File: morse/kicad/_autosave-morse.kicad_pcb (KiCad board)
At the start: 2 copper layers, 63.5 x 63.5 mm, 14 parts, among them J1 Conn_01x04, Q1 2N2219, Q2 2N2219

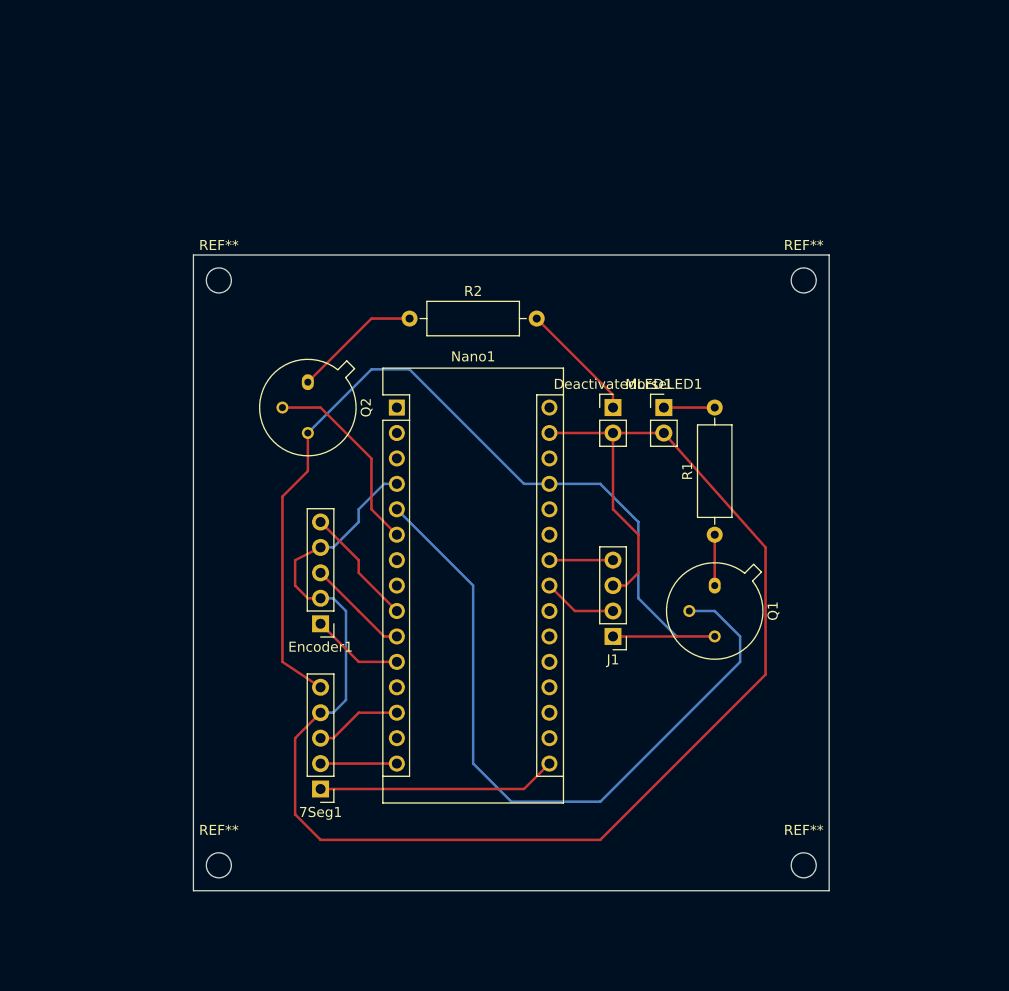
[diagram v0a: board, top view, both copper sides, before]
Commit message: updating maze symlinks and added rotary encoder to kicad
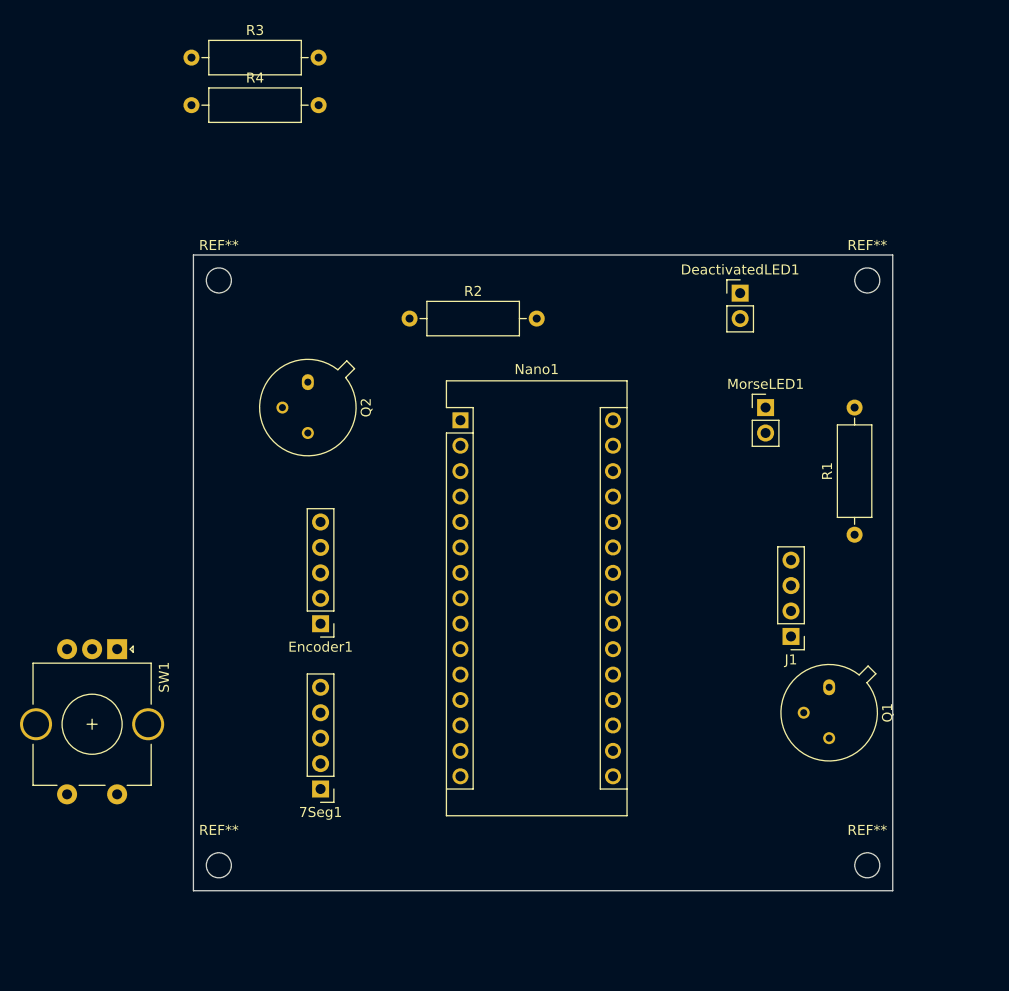
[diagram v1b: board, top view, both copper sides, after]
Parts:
- added R3: R, Resistor_THT:R_Axial_DIN0309_L9.0mm_D3.2mm_P12.70mm_Horizontal, F.Cu at (133.2, 51.4)
- added R4: R, Resistor_THT:R_Axial_DIN0309_L9.0mm_D3.2mm_P12.70mm_Horizontal, F.Cu at (133.2, 56.2)
- added SW1: Rotary_Encoder_Switch, Rotary_Encoder:RotaryEncoder_Alps_EC11E-Switch_Vertical_H20mm_CircularMountingHoles, F.Cu at (125.7, 110.5)
- moved J1 17.8 mm to (193.0, 109.2)
- moved DeactivatedLED1 17.1 mm to (188.0, 74.9)
- moved Q1 15.3 mm to (196.8, 114.3)
- moved R1 14.0 mm to (199.4, 99.1)
- moved MorseLED1 10.2 mm to (190.5, 86.4)
- moved Nano1 6.48 mm to (160.0, 87.6)
- moved REF** 6.35 mm to (200.7, 132.1)
- moved REF** 6.35 mm to (200.7, 73.7)
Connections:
- Nano1 pad 10: Net-(Encoder1-Pad3) -> Net-(Nano1-Pad10)
- Nano1 pad 11: Net-(Encoder1-Pad1) -> Net-(Nano1-Pad11)
- Nano1 pad 9: Net-(Encoder1-Pad5) -> Net-(Nano1-Pad9)
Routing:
- net GND: track 158.1 -> 0.00 mm
- net +5V: track 97.4 -> 0.00 mm
- net Net-(Nano1-Pad5): track 71.3 -> 0.00 mm
- net Net-(7Seg1-Pad1): track 23.9 -> 0.00 mm
- net Net-(Nano1-Pad6): track 19.7 -> 0.00 mm
- net Net-(Q2-Pad1): track 12.8 -> 0.00 mm
- net Net-(DeactivatedLED1-Pad1): track 12.0 -> 0.00 mm
- net Net-(Encoder1-Pad5): track 12.0 -> 0.00 mm
- net Net-(Encoder1-Pad3): track 10.3 -> 0.00 mm
- net Net-(Encoder1-Pad1): track 9.20 -> 0.00 mm
- net Net-(7Seg1-Pad3): track 8.67 -> 0.00 mm
- net Net-(7Seg1-Pad2): track 7.62 -> 0.00 mm
- net Net-(J1-Pad2): track 7.40 -> 0.00 mm
- net Net-(J1-Pad4): track 6.35 -> 0.00 mm
- net Net-(Q1-Pad1): track 5.08 -> 0.00 mm
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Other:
- board size 63.5 x 63.5 mm -> 69.8 x 63.5 mm

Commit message: started adding knob module, started adding timing into master
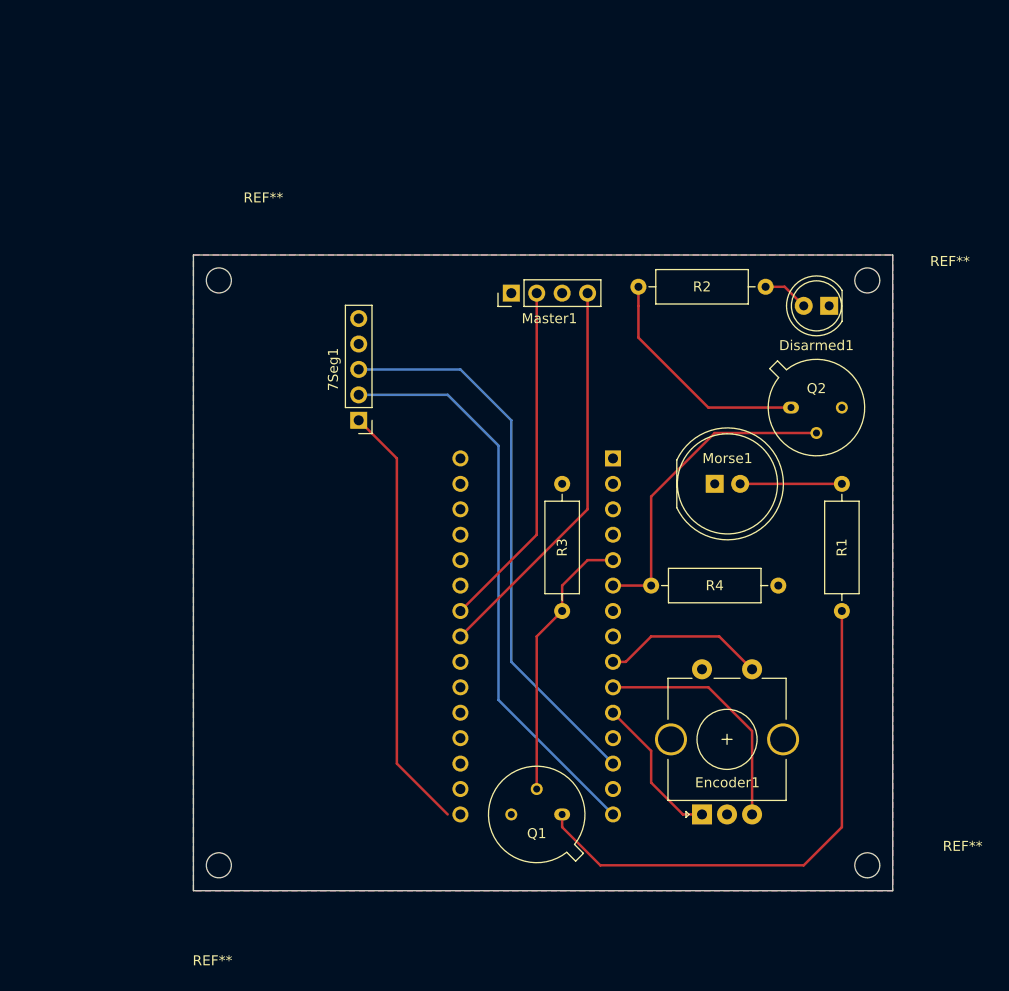
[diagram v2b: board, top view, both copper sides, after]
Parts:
- removed DeactivatedLED1, MorseLED1: Conn_01x02, Connector_PinHeader_2.54mm:PinHeader_1x02_P2.54mm_Vertical
- removed the Encoder1 at (146.1, 108.0)
- added Disarmed1: LED, LED_THT:LED_D5.0mm, F.Cu at (196.8, 76.2)
- added Morse1: LED, LED_THT:LED_D10.0mm, F.Cu at (185.4, 94.0)
- Nano1: moved to B.Cu
- moved R3 66.5 mm to (170.2, 106.7), turned to 90 degrees
- moved R4 66.4 mm to (179.1, 104.1)
- moved Encoder1 60.7 mm to (184.2, 127.0), turned to 90 degrees
- moved Q2 48.3 mm to (193.0, 86.4), turned to 0 degrees
- moved Master1 44.2 mm to (165.1, 74.9), turned to 90 degrees
- moved 7Seg1 37.0 mm to (149.9, 87.6)
- moved Q1 29.5 mm to (170.2, 127.0), turned to 180 degrees
- moved R2 23.1 mm to (177.8, 74.3)
- moved Nano1 15.7 mm to (175.3, 91.4), turned to 180 degrees
- moved R1 7.73 mm to (198.1, 106.7)
- renumbered SW1 to Encoder1, J1 to Master1
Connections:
- Encoder1 pad A: Net-(Nano1-Pad10) -> Net-(Encoder1-PadA)
- Encoder1 pad B: Net-(Nano1-Pad11) -> Net-(Encoder1-PadB)
- Master1 pad 2: Net-(J1-Pad2) -> Net-(Master1-Pad2)
- Master1 pad 4: Net-(J1-Pad4) -> Net-(Master1-Pad4)
- Nano1 pad 10: Net-(Nano1-Pad10) -> Net-(Encoder1-PadB)
- Nano1 pad 11: Net-(Nano1-Pad11) -> Net-(Encoder1-PadA)
- Nano1 pad 23: Net-(J1-Pad2) -> Net-(Master1-Pad4)
- Nano1 pad 24: Net-(J1-Pad4) -> Net-(Master1-Pad2)
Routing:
- net Net-(7Seg1-Pad2): track 0.00 -> 57.6 mm
- net Net-(7Seg1-Pad3): track 0.00 -> 55.8 mm
- net Net-(Q1-Pad1): track 0.00 -> 54.0 mm
- net Net-(7Seg1-Pad1): track 0.00 -> 43.1 mm
- net Net-(Master1-Pad4): track 0.00 -> 39.6 mm
- net Net-(Master1-Pad2): track 0.00 -> 34.9 mm
- net Net-(Nano1-Pad6): track 0.00 -> 31.8 mm
- net Net-(Nano1-Pad5): track 0.00 -> 27.5 mm
- net Net-(Encoder1-PadB): track 0.00 -> 24.0 mm
- net Net-(Q2-Pad1): track 0.00 -> 23.2 mm
- net Net-(Encoder1-PadS1): track 0.00 -> 16.3 mm
- net Net-(Encoder1-PadA): track 0.00 -> 15.0 mm
- net Net-(Morse1-Pad2): track 0.00 -> 10.2 mm
- net Net-(Disarmed1-Pad2): track 0.00 -> 4.60 mm
- added copper zone on F.Cu, net +5V
- added copper zone on B.Cu, net GND
